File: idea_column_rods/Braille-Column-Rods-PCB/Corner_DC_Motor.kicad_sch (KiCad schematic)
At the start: 9 parts, among them M9 Motor_DC_With_MP, U10 AD116, U25 MT910xET

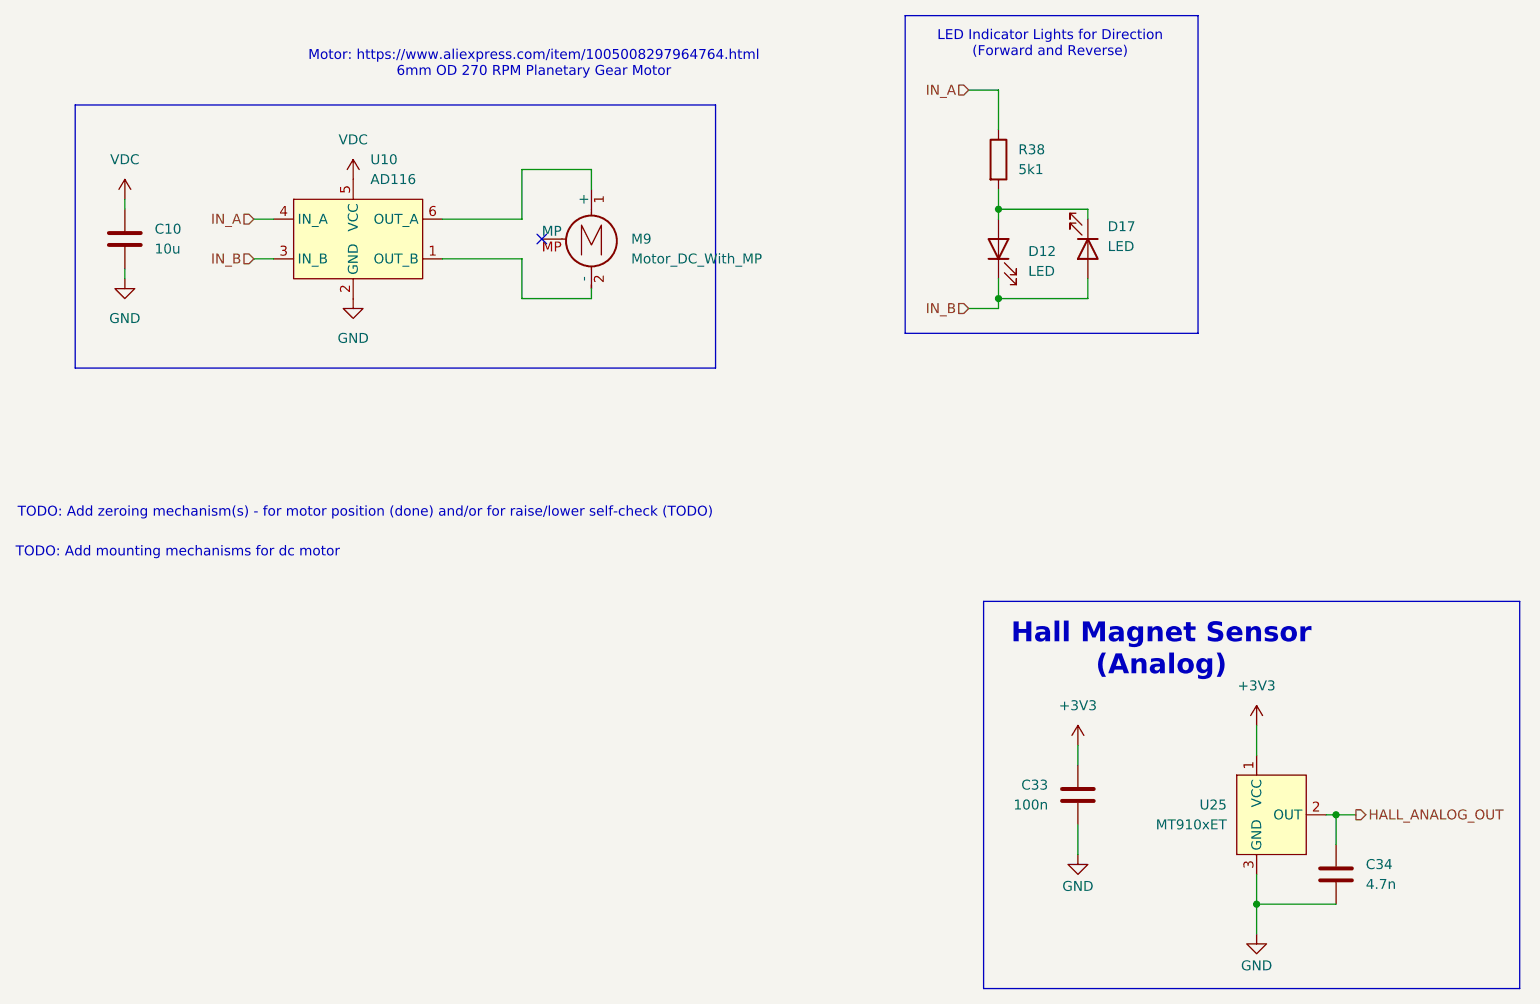
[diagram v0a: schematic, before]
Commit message: Create PCB and CAD for Type 4 Rev 1 rod cams (#13)
* WIP: Rods PCB placement

* WIP: Place the housing and motor X

* WIP: Position everything

* WIP: Update tight placement of DC motor

* WIP: Layout and route the stepper driver

* WIP: Motor layout is good

* WIP: Manual routing and silkscreens

* Comments

* Big routing

* Clean up DRC (mostly footprints)

* Fix spacing issue on top

* Fix spacing issues on bottom

* Create render of 6mm motor, add to PCB

* WIP: Get cams good

* WIP: Reorder the cam bushing and hall sensor

* Finish and tag release

* Complete type 4 rev 1

* Create dc_motor_clamp cad
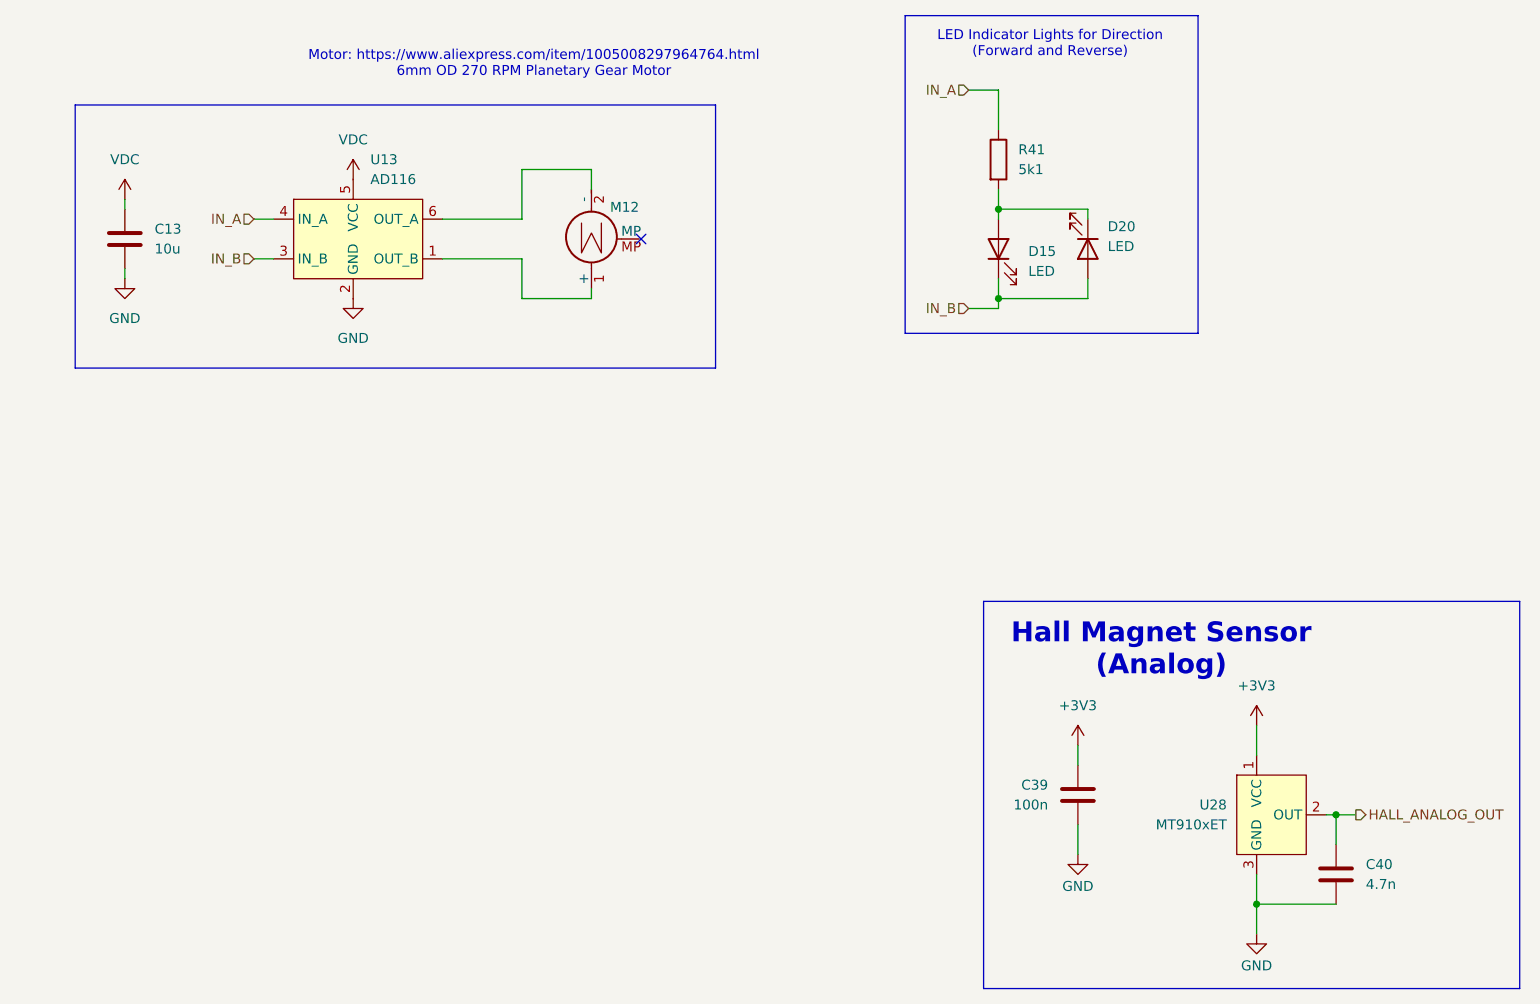
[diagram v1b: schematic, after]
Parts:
- U28: renamed from U25; footprint Package_TO_SOT_SMD:SOT-23 -> 00-lib-footprints:SOT-23-Hall
- renumbered C10 to C13, C33 to C39, C34 to C40, D12 to D15, D17 to D20, M9 to M12, R38 to R41, U10 to U13
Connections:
- net at M12.1 (+): now also U13.1 (OUT_B); no longer U13.6 (OUT_A)
- net at M12.2 (-): now also U13.6 (OUT_A); no longer U13.1 (OUT_B)
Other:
- note removed: "TODO: Add mounting mechanisms for dc motor"
- note removed: "TODO: Add zeroing mechanism(s) - for motor position (done) and/or for raise/lower self-check (TODO)"
- title: (none) -> Braille Cam Rod Prototype (Type 4)
- moved on the sheet: M12
